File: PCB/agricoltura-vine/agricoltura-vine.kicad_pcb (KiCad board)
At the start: 2 copper layers, 100 x 60 mm, 103 parts, among them SW1 B3U-1000P, SW2 CVS-02TB, SW3 CVS-02TB, SW4 CVS-02TB, SW5 CVS-02TB, T1 BU2032SM-JJ-GTR, T10 BM04B-SRSS-TB(LF)(SN), T11 BM04B-SRSS-TB(LF)(SN), T12 BM04B-SRSS-TB(LF)(SN), T13 BM04B-SRSS-TB(LF)(SN), T14 BM04B-SRSS-TB(LF)(SN), T15 BM04B-SRSS-TB(LF)(SN), T16 1755736, T17 RJHSE-5381, T18 RJHSE-5381, T19 TSW-108-07-G-T, T2 20021121-00010C4LF, T20 TSW-108-07-G-T, T3 0675031020, T4 BM04B-SRSS-TB(LF)(SN), T5 BM04B-SRSS-TB(LF)(SN), T6 BM04B-SRSS-TB(LF)(SN), T7 BM04B-SRSS-TB(LF)(SN), T8 BM04B-SRSS-TB(LF)(SN), T9 BM04B-SRSS-TB(LF)(SN), U1 STM32F446RET6, U2 74HC4052D, U3 TCA9548APWR, U4 AP63203WU-7, U5 AP63205WU-7, U6 MAX3073EESD+, U7 MAX3073EESD+, U8 SN74LV541APWR, U9 TXB0108PWR, X1 ABM3B-8.000MHZ-B2-T, X2 ABS07-32.768KHZ-9-T

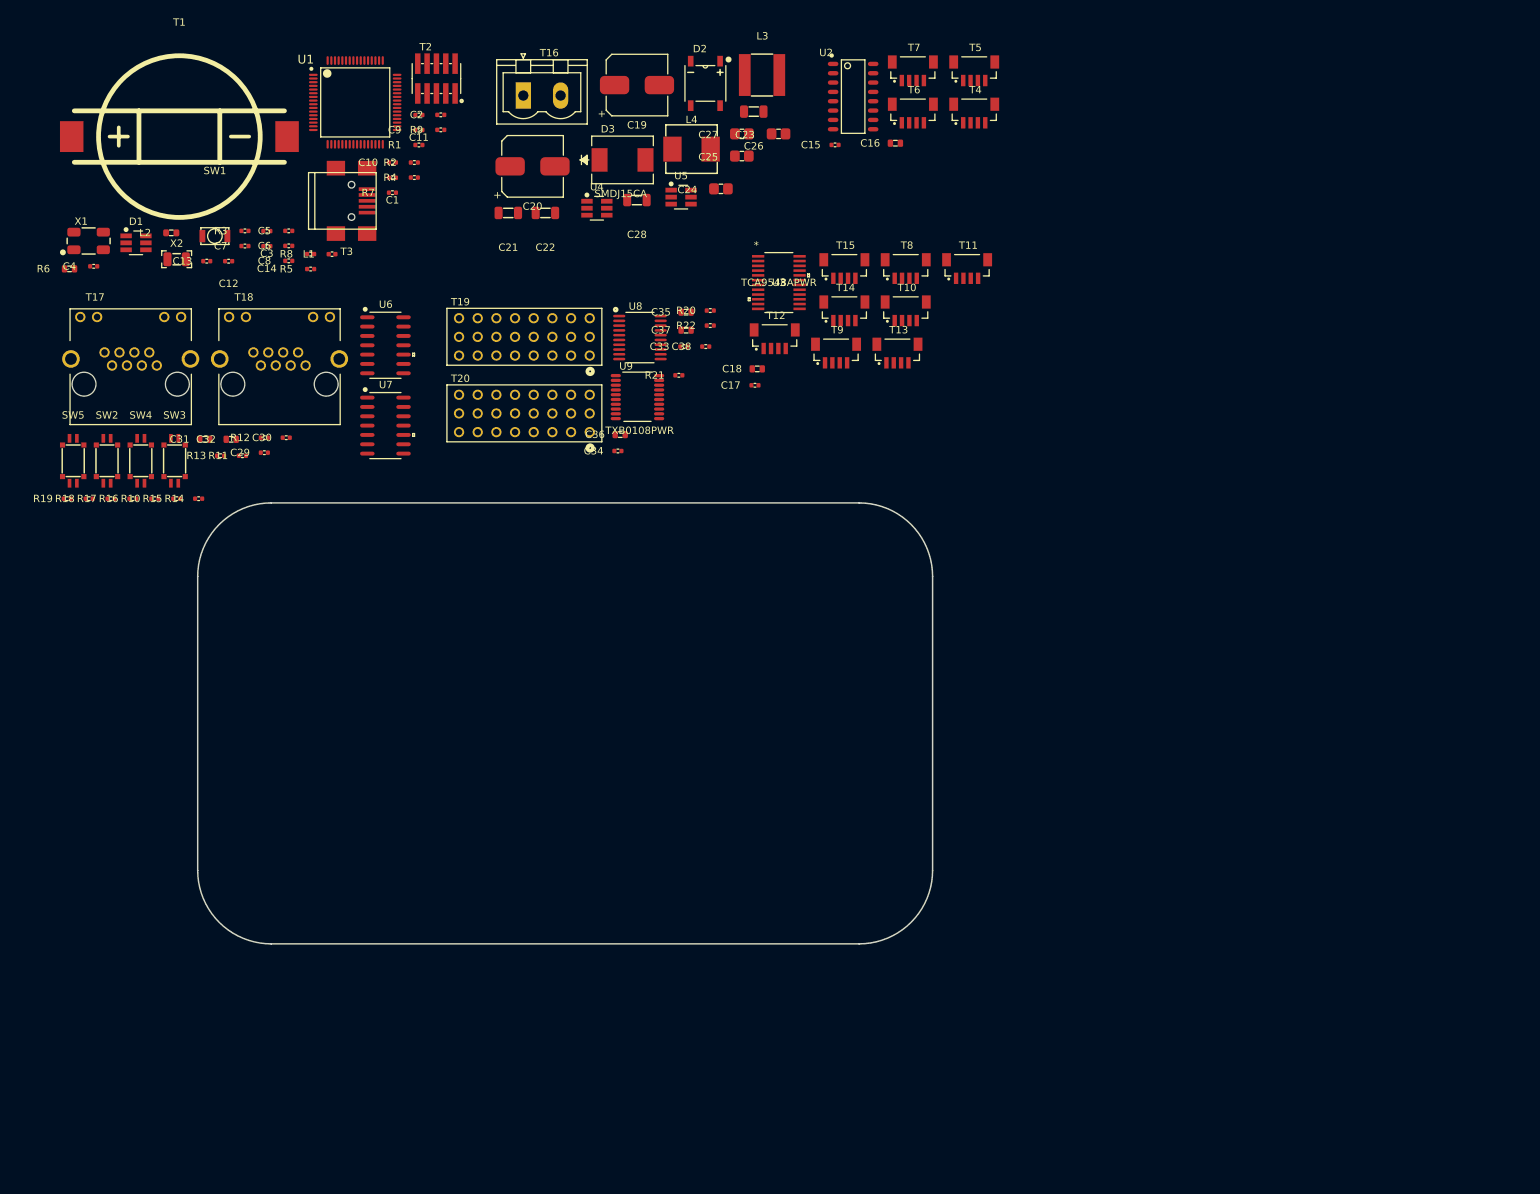
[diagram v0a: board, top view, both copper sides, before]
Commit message: Board Size , Connectors and Layout
Changed board size and shape, started layout, swapped connectors over.
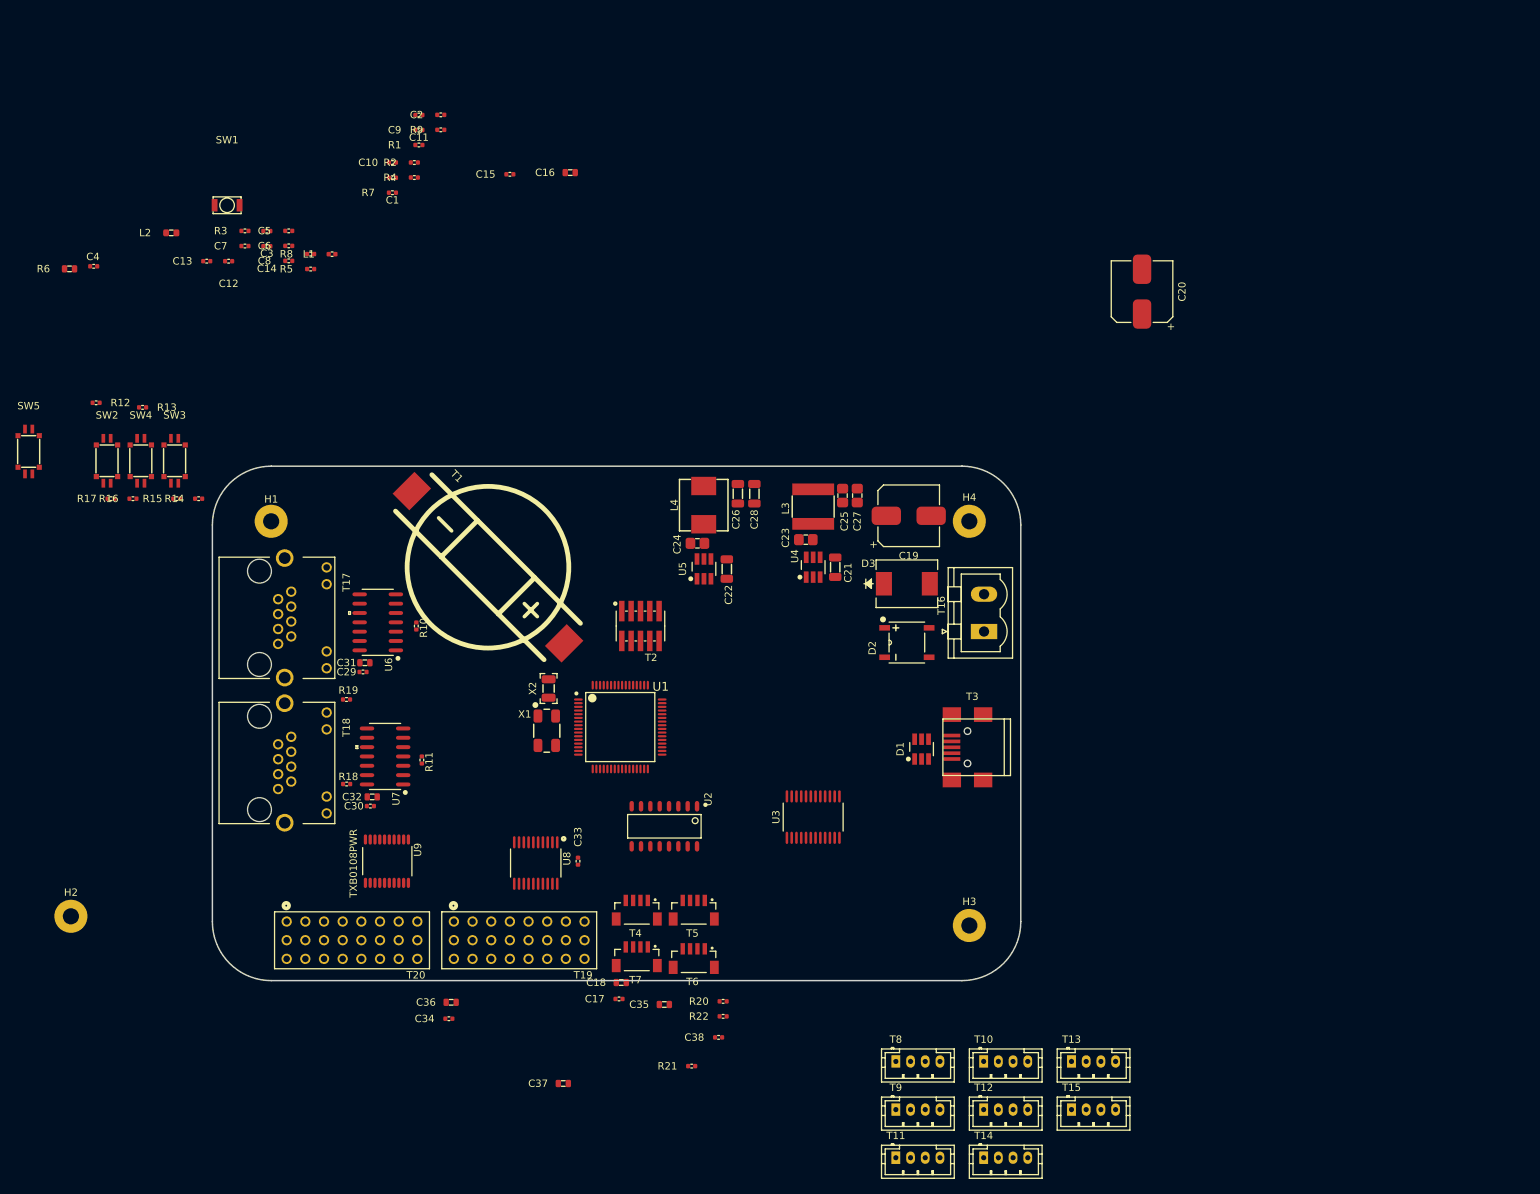
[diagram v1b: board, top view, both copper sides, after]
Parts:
- added H1: M2_Plated_Hole, AVR-KiCAD-Lib-Holes_Fasteners:M2_HOLE, F.Cu at (110.0, 72.5)
- added H2: M2_Plated_Hole, AVR-KiCAD-Lib-Holes_Fasteners:M2_HOLE, F.Cu at (82.8, 126.2)
- added H3: M2_Plated_Hole, AVR-KiCAD-Lib-Holes_Fasteners:M2_HOLE, F.Cu at (205.0, 127.5)
- added H4: M2_Plated_Hole, AVR-KiCAD-Lib-Holes_Fasteners:M2_HOLE, F.Cu at (205.0, 72.5)
- T10, T11, T12, T13, T14, T15, T8, T9: value BM04B-SRSS-TB(LF)(SN) -> B4B-PH-K-S(LF)(SN); footprint AVR-KiCAD-Lib-Connectors:CONN_BM04B-SRSS-TB(LF)(SN) -> AVR-KiCAD-Lib-Connectors:B4B-PH-K-S(LF)(SN)
- moved D1 127.2 mm to (198.5, 103.5), turned to 90 degrees
- moved T7 126.3 mm to (159.8, 131.8), turned to 180 degrees
- moved T11 121.4 mm to (195.0, 159.1)
- moved T5 120.4 mm to (167.5, 125.4), turned to 180 degrees
- moved T6 118.8 mm to (167.5, 132.0), turned to 180 degrees
- moved T15 118.5 mm to (218.9, 152.6)
- moved T4 117.8 mm to (159.8, 125.4), turned to 180 degrees
- moved T14 116.8 mm to (206.9, 159.1)
- moved T3 112.0 mm to (204.8, 103.2), turned to 180 degrees
- moved T12 108.7 mm to (206.9, 152.6)
- moved T8 107.9 mm to (195.0, 146.0)
- moved C37 103.9 mm to (149.8, 149.0)
- moved T9 103.3 mm to (195.0, 152.6)
- moved T10 102.7 mm to (206.9, 146.0)
- moved U2 102.6 mm to (163.5, 114.0), turned to 270 degrees
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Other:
- board size 100 x 60 mm -> 110 x 70 mm

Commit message: Board shape and Rough PLacement
Board shape adjusted to have smaller rounded corners increasing usable space of board shape. Finished rough placement of all the components, no routing yet. Debating connector style and form factor. Right now supports Seeedstudio grove connectors, contemplating Sparkfun Qwiic  and Adafruit Stemma connectors as alternatives or including a variety of all 3.
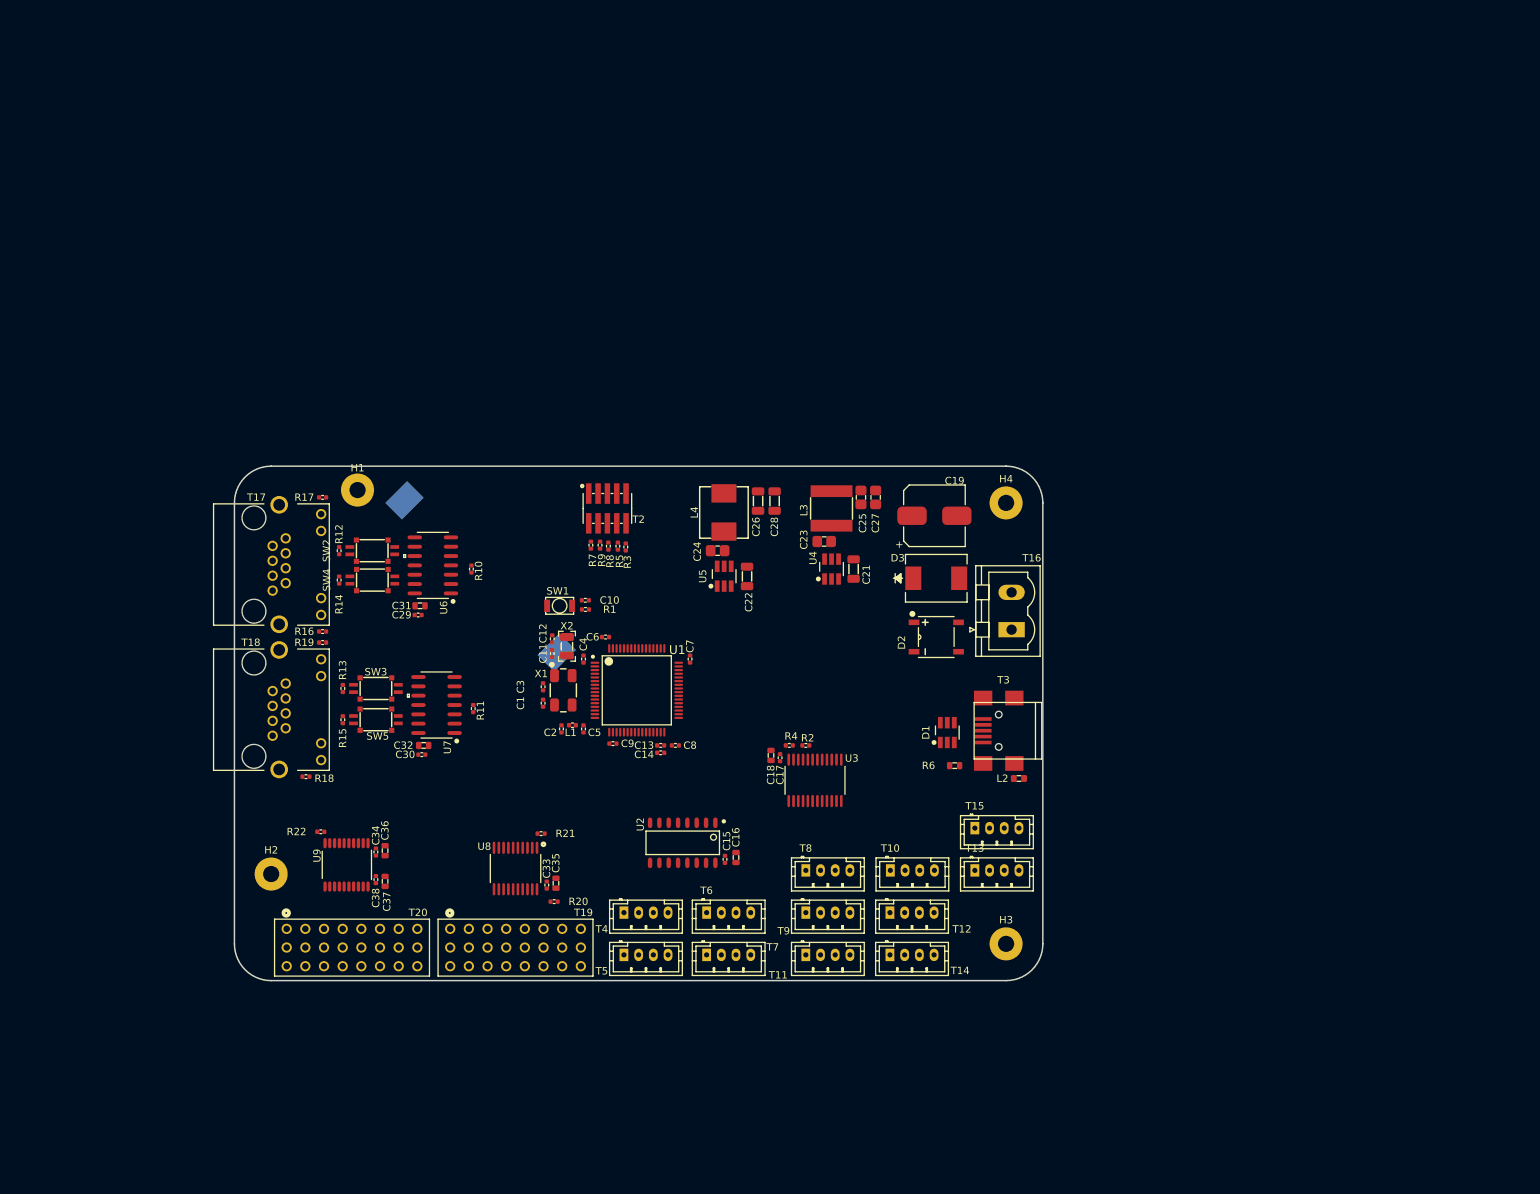
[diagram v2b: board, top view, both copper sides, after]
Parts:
- removed C20: UUQ1H470MCL1GS, AVR-KiCAD-Lib-Capacitors:CP_Elec_8x10
- T1: moved to B.Cu
- T4, T5, T6, T7: value BM04B-SRSS-TB(LF)(SN) -> B4B-PH-K-S(LF)(SN); footprint AVR-KiCAD-Lib-Connectors:CONN_BM04B-SRSS-TB(LF)(SN) -> AVR-KiCAD-Lib-Connectors:B4B-PH-K-S(LF)(SN)
- moved R6 138.1 mm to (203.0, 105.8)
- moved L2 137.2 mm to (211.8, 107.5)
- moved C15 97.7 mm to (171.8, 118.5), turned to 90 degrees
- moved C16 95.9 mm to (173.2, 118.2), turned to 90 degrees
- moved R2 95.5 mm to (182.8, 103.0), turned to 180 degrees
- moved R4 92.6 mm to (180.5, 103.0)
- moved C13 90.3 mm to (163.0, 103.0)
- moved C9 87.6 mm to (156.5, 102.8), turned to 180 degrees
- moved C14 87.3 mm to (163.0, 104.0)
- moved C4 85.4 mm to (152.5, 91.2), turned to 90 degrees
- moved C2 85.2 mm to (149.5, 100.8), turned to 270 degrees
- moved C8 84.4 mm to (165.0, 103.0)
- moved C7 82.6 mm to (167.0, 91.2), turned to 90 degrees
- moved C5 78.7 mm to (152.5, 100.8), turned to 270 degrees
- moved C11 75.5 mm to (148.2, 90.5), turned to 270 degrees
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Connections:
- C33 pad 1: +3V3 -> +5V
- C35 pad 1: +3V3 -> +5V
- U8 pad 11: Net-(T19-Pad22) -> Net-(T19-Pad1)
- U8 pad 12: Net-(T19-Pad19) -> Net-(T19-Pad4)
- U8 pad 13: Net-(T19-Pad16) -> Net-(T19-Pad7)
- U8 pad 14: Net-(T19-Pad13) -> Net-(T19-Pad10)
- U8 pad 15: Net-(T19-Pad10) -> Net-(T19-Pad13)
- U8 pad 16: Net-(T19-Pad7) -> Net-(T19-Pad16)
- U8 pad 17: Net-(T19-Pad4) -> Net-(T19-Pad19)
- U8 pad 18: Net-(T19-Pad1) -> Net-(T19-Pad22)
- U8 pad 20: +3V3 -> +5V
- U9 pad 12: Net-(T20-Pad22) -> Net-(T20-Pad1)
- U9 pad 13: Net-(T20-Pad19) -> Net-(T20-Pad4)
- U9 pad 14: Net-(T20-Pad16) -> Net-(T20-Pad7)
- U9 pad 15: Net-(T20-Pad13) -> Net-(T20-Pad10)
- U9 pad 16: Net-(T20-Pad10) -> Net-(T20-Pad13)
- U9 pad 17: Net-(T20-Pad7) -> Net-(T20-Pad16)
- U9 pad 18: Net-(T20-Pad4) -> Net-(T20-Pad19)
- U9 pad 20: Net-(T20-Pad1) -> Net-(T20-Pad22)
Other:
- outline, holes or cut-outs redrawn
